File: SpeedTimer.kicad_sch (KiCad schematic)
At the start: 4 parts, among them Y1 ASCO

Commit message: Added 3.3v LDO. Increased page size. Added start/stop button circuit
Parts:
- added C2: 1n, symbol Device:C
- added C3: 2.2u, symbol Device:C
- added C4: .1u, symbol Device:C
- added D1: LED, symbol Device:LED
- added R10, R11, R3: 10K, symbol Device:R
- added R4: 600K, symbol Device:R
- added R5, R8: 1M, symbol Device:R
- added R6, R7: 47K, symbol Device:R
- added R9: 470, symbol Device:R
- added SW1, SW2, SW3: SW_Push, symbol Switch:SW_Push
- added U1, U2: 74LS393, symbol 74xx:74LS393
- added U3: 74HC74, symbol 74xx:74HC74
- added U4: KM28C64A, Package_DIP:DIP-28_W15.24mm, symbol Memory_EEPROM:KM28C64A
- added U5: 74HC173, symbol 74xx:74HC173
- added U6: LM317L_TO92, Package_TO_SOT_THT:TO-92_Inline, symbol Regulator_Linear:LM317L_TO92
- added U7: 74LS08, symbol 74xx:74LS08
- added U8: 74HC14, symbol 74xx:74HC14
- R1: value 1k -> 1K
- R2: value 1k -> 10K
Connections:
- net GND: now also C3.1, C4.1, D1.1 (K), R10.2, R11.2, R3.1, R5.2, R7.1, U1.7 (GND), U2.7 (GND), U3.7 (GND), U7.7 (GND), U8.7 (GND)
- net VDD: now also U1.14 (VCC), U2.14 (VCC), U3.14 (VCC), U7.14 (VCC), U8.14 (VCC); no longer R2.2, Y1.4 (VDD)
- net at C1.2, R1.1: now also R6.1, R7.2
- net at R1.2: now also U1.1 (CP)
- net CLK_32.768MHz: now reaches C1.1, Y1.3 (OUT)
- new net: R10.1, SW1.2, U7.4
- new net: U8.2, U8.3
- new net: U7.1, U8.4
- new net: R4.1, R5.1, U6.1 (ADJ)
- new net: C2.1, R3.2, U1.12 (MR), U1.2 (MR)
- new net: R8.2, R9.1, U7.10, U7.6
- new net: D1.2 (A), R9.2
- new net: C3.2, R8.1, U8.1
- new net: R11.1, SW2.2, U7.5
- new net: U1.13 (CP), U1.6 (Q3)
- new net +3.3V: C4.2, R2.2, R4.2, U6.2 (VO), Y1.4 (VDD)
- new net +5V: C2.2, R6.2, SW1.1, SW2.1, U3.4 (~{S}), U6.3 (VI)
- new net CLK_1kHz: U1.9 (Q2)
- new net SIG_START: U7.3
- new net SIG_STOP: U7.8
- new net TIMER_RUNNING: U3.5 (Q), U7.9
- new net ~{TIMER_RUNNING}: U3.2 (D), U3.6 (~{Q}), U7.2
- no-connect marks 0 -> 6
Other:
- moved on the sheet: C1, R1, R2, Y1

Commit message: Updated some triggering criteria
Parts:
- added C5, C6, C7: 1n, symbol Device:C
- added D4: LED, symbol Device:LED
- added Q1: NPN, symbol Simulation_SPICE:NPN
- added R12: 470, symbol Device:R
- added R13, R14, R15: 10K, symbol Device:R
- added U9: 74HC14, symbol 74xx:74HC14
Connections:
- net +3.3V: now also Q1.1 (C); no longer R2.2
- net +5V: now also SW3.1, U3.10 (~{S}), U3.12 (D), R13.1
- net GND: now also R2.1, R3.2, R9.2, R12.2, R14.2, R15.2; no longer D1.1 (K), R3.1
- net SIG_START: now also U8.6; no longer U7.3
- net SIG_STOP: now also C7.1, R14.1; no longer U7.8
- net TIMER_RUNNING: now also Q1.2 (B)
- net RESET: now reaches C2.1, U1.12 (MR), U1.2 (MR)
- net RESET: now also SW3.2, R15.1, U9.1; no longer R3.2
- net at R8.2, U7.10, U7.6: now also D1.2 (A); no longer R9.1
- net SIG_READY: now reaches U3.11 (C)
- net SIG_READY: now also R3.1, C5.1
- net ~{RESET}: now reaches U3.13 (~{R})
- net ~{RESET}: now also U3.1 (~{R}), U9.2
- net INIT: now reaches U3.8 (~{Q})
- net INIT: now also U7.13
- net READY: now reaches U3.9 (Q)
- net at U8.5: now also C6.1, R13.2
- net at Y1.1 (Tri-State): now also R2.2, Q1.3 (E); no longer R2.1
- net at U7.11: now also C5.2, C6.2, D4.2 (A)
- net at U7.12: now also U7.3
- new net: D1.1 (K), R9.1
- new net: C7.2, U7.8
- new net: D4.1 (K), R12.1
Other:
- moved on the sheet: C3, D1, R8, R9, U1B, U3A, U3B, U5, U7C, U7D, U8B, U8C

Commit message: Updated placement
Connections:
- net at C5.2, D4.2 (A), U7.11: no longer C6.2
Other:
- moved on the sheet: C2, C3, C5, C6, C7, D1, D4, R10, R11, R12, R13, R14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

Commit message: Filled out timer counter and started building out ALU
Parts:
- added D2, D3, D5, D6: D, symbol Device:D
- added R16: 10K, symbol Device:R
- added U10, U13: 74LS393, symbol 74xx:74LS393
- added U11, U12: CD4051B, symbol Analog_Switch:CD4051B
- added U14, U15: 74LS283, symbol 74xx:74LS283
- added U16: 74HC173, symbol 74xx:74HC173
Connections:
- net +3.3V: now also R16.2; no longer Q1.1 (C)
- net +5V: now also Q1.1 (C), U4.27 (~{WE}), U4.28 (VCC), U5.16 (VCC), U11.16 (VDD), U12.16 (VDD), U14.16 (VCC), U16.16 (VCC)
- net CLK_1kHz: now also U2.1 (CP)
- net CLK_32.768MHz: now also U5.7 (Cp), U13.1 (CP), U16.7 (Cp)
- net GND: now also D1.1 (K), D4.1 (K), U4.14 (GND), U4.2 (A12), U4.20 (~{CE}), U4.21 (A10), U4.22 (~{OE}), U4.23 (A11), U4.24 (A9), U4.25 (A8), U5.1 (Oe1), U5.10 (E2), U5.2 (Oe2), U5.8 (GND), U5.9 (E1), U10.7 (GND), U11.7 (VEE), U11.8 (VSS), U12.7 (VEE), U12.8 (VSS), U13.12 (MR), U13.2 (MR), U13.7 (GND), U14.8 (GND), U16.1 (Oe1), U16.10 (E2), U16.2 (Oe2), U16.8 (GND), U16.9 (E1); no longer R12.2, R9.2
- net INIT: now also D2.2 (A); no longer U7.13
- net READY: now also U7.1, D3.2 (A)
- net RESET: now also U2.12 (MR), U2.2 (MR), U10.12 (MR), U10.2 (MR); no longer U1.12 (MR), U1.2 (MR)
- net SIG_START: now also D5.2 (A)
- net SIG_STOP: now also D6.2 (A)
- net TIMER_RUNNING: no longer Q1.2 (B)
- net VDD: now also U10.14 (VCC), U13.14 (VCC)
- net ~{TIMER_RUNNING}: now also Q1.2 (B); no longer U7.2
- net at U8.4: now also C5.2, R12.1; no longer U7.1
- net at U2.10 (Q1): now also U11.5 (X5)
- net at U2.11 (Q0): now also U11.1 (X4)
- net at U2.13 (CP): now also U2.6 (Q3), U11.12 (X3)
- net at U2.8 (Q3): now also U10.1 (CP), U11.4 (X7)
- net at U2.9 (Q2): now also U11.2 (X6)
- net at R9.1: now also U7.10, U7.13, U7.6; no longer D1.1 (K)
- net at U5.11 (D3): now also U14.10 (S4)
- net at U5.12 (D2): now also U14.13 (S3)
- net at U5.13 (D1): now also U14.1 (S2)
- net at U5.14 (D0): now also U14.4 (S1)
- net at Q1.3 (E), R2.2: now also U1.12 (MR), U1.2 (MR); no longer Y1.1 (Tri-State)
- net at C6.2: now also U7.3
- net at U3.3 (C): now also D5.1 (K), D6.1 (K)
- net at U8.8: now also U12.6 (INH)
- net at U8.9: now also U4.7 (A3), U11.6 (INH), U13.13 (CP), U13.6 (Q3)
- net at U4.10 (A0): now also U11.11 (A), U12.11 (A), U13.3 (Q0)
- net at U4.11 (I/O0): now also U14.5 (A1)
- net at U4.12 (I/O1): now also U14.3 (A2)
- net at U4.13 (I/O2): now also U14.14 (A3)
- net at U4.15 (I/O3): now also U14.12 (A4)
- net at U4.3 (A7): now also U13.8 (Q3)
- net at U4.4 (A6): now also U13.9 (Q2)
- net at U4.5 (A5): now also U13.10 (Q1)
- net at U4.6 (A4): now also U13.11 (Q0)
- net at U4.8 (A2): now also U11.9 (C), U12.9 (C), U13.5 (Q2)
- net at U4.9 (A1): now also U11.10 (B), U12.10 (B), U13.4 (Q1)
- net at U2.3 (Q0): now also U11.13 (X0)
- net at U2.4 (Q1): now also U11.14 (X1)
- net at U2.5 (Q2): now also U11.15 (X2)
- net at U7.12: now also D2.1 (K), D3.1 (K); no longer U7.3
- net at U8.10: now also U7.2
- net at U8.11: now also R8.2, U7.11
- new net: U10.10 (Q1), U12.5 (X5)
- new net: U10.11 (Q0), U12.1 (X4)
- new net: U10.13 (CP), U10.6 (Q3), U12.12 (X3)
- new net: U10.8 (Q3), U12.4 (X7)
- new net: U10.9 (Q2), U12.2 (X6)
- new net: D1.2 (A), R9.2
- new net: R16.1, Y1.1 (Tri-State)
- new net: U10.3 (Q0), U12.13 (X0)
- new net: U10.4 (Q1), U12.14 (X1)
- new net: U10.5 (Q2), U12.15 (X2)
- new net: D4.2 (A), R12.2
- new net CURRENT_BIT: U11.3 (X), U12.3 (X)
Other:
- note added: "3.3V LDO"
- note added: "Clock Divider"
- note added: "Timer Counter"
- note added: "Timer Ready Control Bit"
- note added: "Timer Run Control Bit"
- note added: "Timer Start Control Flow"
- moved on the sheet: C1, C2, C3, C4, C5, C6, C7, D1, D4, Q1, R1, R10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

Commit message: Figured out ALU alignment
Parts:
- added U17: 74HC173, symbol 74xx:74HC173
- added U18: 74LS08, symbol 74xx:74LS08
- added U19: HDSP-7401, Display_7Segment:HDSP-7401, symbol Display_Character:HDSP-7401
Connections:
- net CURRENT_BIT is gone; now on an unnamed net: U11.3 (X), U12.3 (X)
- net +5V: now also U15.16 (VCC), U17.16 (VCC)
- net CLK_32.768MHz: now also U16.1 (Oe1), U5.1 (Oe1)
- net GND: now also U15.11 (B4), U15.12 (A4), U15.14 (A3), U15.15 (B3), U15.2 (B2), U15.3 (A2), U15.6 (B1), U15.8 (GND), U16.15 (Mr), U16.4 (Q1), U16.5 (Q2), U16.6 (Q3), U5.15 (Mr), U17.1 (Oe1), U17.10 (E2), U17.15 (Mr), U17.2 (Oe2), U17.8 (GND), U17.9 (E1), U18.7 (GND); no longer U16.1 (Oe1), U4.22 (~{OE}), U5.1 (Oe1)
- net VDD: now also U18.14 (VCC)
- net at U14.11 (B4): now also U5.6 (Q3), U17.11 (D3)
- net at U14.15 (B3): now also U5.5 (Q2), U17.12 (D2)
- net at U14.2 (B2): now also U5.4 (Q1), U17.13 (D1)
- net at U14.6 (B1): now also U5.3 (Q0), U17.14 (D0)
- net at U14.9 (C4): now also U15.7 (C0)
- net at U13.10 (Q1), U4.5 (A5): now also U18.2
- net at U13.9 (Q2), U4.4 (A6): now also U18.1
- net at U16.11 (D3): now also U15.10 (S4)
- net at U16.12 (D2): now also U15.13 (S3)
- net at U16.13 (D1): now also U15.1 (S2)
- net at U16.14 (D0): now also U15.4 (S1)
- net at U16.3 (Q0): now also U15.5 (A1)
- net at U8.12: now also U4.22 (~{OE})
- new net: U17.7 (Cp), U18.3
- no-connect marks 6 -> 10
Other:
- moved on the sheet: U13B, U15, U16, U5, U8F, U8G

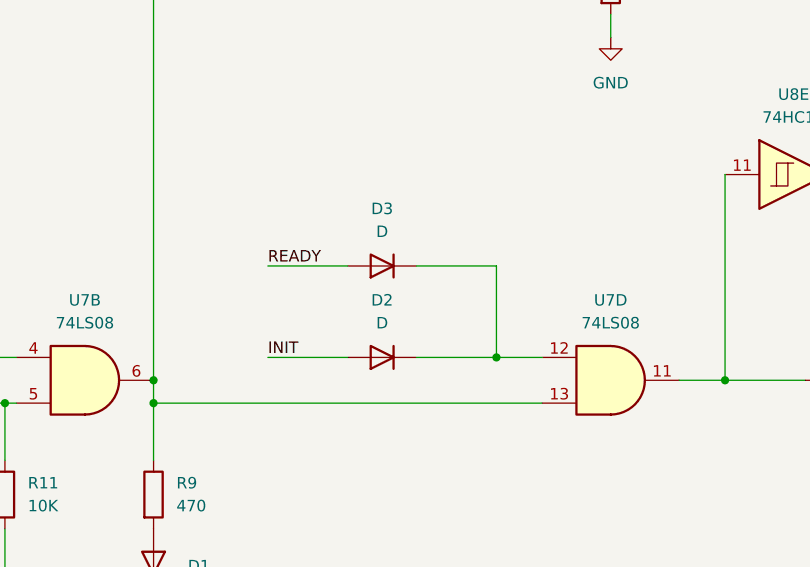
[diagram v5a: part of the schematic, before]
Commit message: Updated gitignore to ignore -bak files
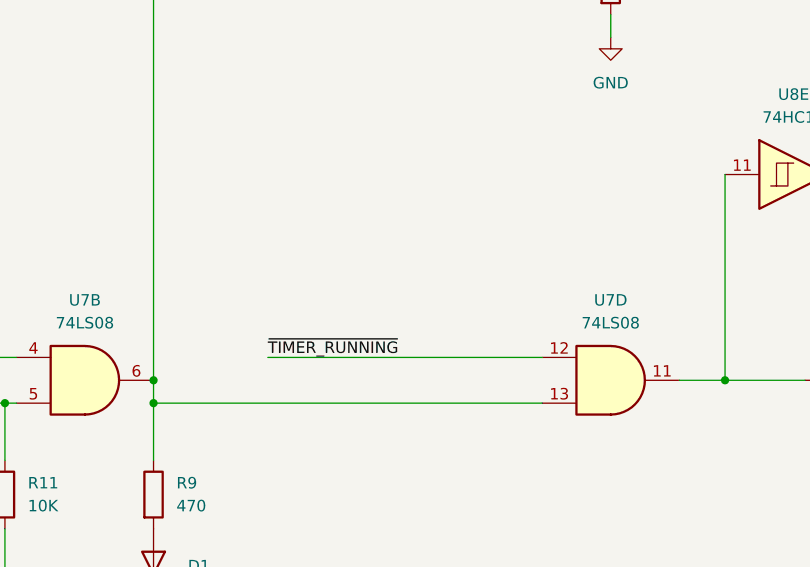
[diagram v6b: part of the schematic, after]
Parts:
- removed D2, D3: D, symbol Device:D
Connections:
- net ~{TIMER_RUNNING}: now also U7.12
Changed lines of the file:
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@@
 	)
 	(junction
-		(at 101.6 365.76)
-		(diameter 0)
-		(color 0 0 0 0)
-	)
-	(junction
 		(at 408.94 182.88)
 		(diameter 0)
@@
 	(wire
 		(pts
-			(xy 85.09 365.76) (xy 76.2 365.76)
-		)
-		(stroke
-			(width 0)
-			(type default)
-		)
-	)
-	(wire
-		(pts
 			(xy 317.5 111.76) (xy 322.58 111.76)
 		)
@@
 	(wire
 		(pts
-			(xy 101.6 365.76) (xy 106.68 365.76)
-		)
-		(stroke
-			(width 0)
-			(type default)
-		)
-	)
-	(wire
-		(pts
 			(xy 337.82 -29.21) (xy 327.66 -29.21)
 		)
@@
 	(wire
 		(pts
-			(xy 92.71 355.6) (xy 101.6 355.6)
-		)
-		(stroke
-			(width 0)
-			(type default)
-		)
-	)
-	(wire
-		(pts
 			(xy 323.85 151.13) (xy 322.58 151.13)
 		)
@@
 	(wire
 		(pts
-			(xy 92.71 365.76) (xy 101.6 365.76)
-		)
-		(stroke
-			(width 0)
-			(type default)
-		)
-	)
-	(wire
-		(pts
 			(xy 208.28 342.9) (xy 203.2 342.9)
 		)
@@
 	(wire
 		(pts
+			(xy 76.2 365.76) (xy 106.68 365.76)
+		)
+		(stroke
+			(width 0)
+			(type default)
+		)
+	)
+	(wire
+		(pts
 			(xy 50.8 38.1) (xy 63.5 38.1)
 		)
@@
 	(wire
 		(pts
-			(xy 76.2 355.6) (xy 85.09 355.6)
-		)
-		(stroke
-			(width 0)
-			(type default)
-		)
-	)
-	(wire
-		(pts
 			(xy 419.1 177.8) (xy 406.4 177.8)
 		)
@@
 	(wire
 		(pts
-			(xy 101.6 355.6) (xy 101.6 365.76)
-		)
-		(stroke
-			(width 0)
-			(type default)
-		)
-	)
-	(wire
-		(pts
 			(xy 58.42 134.62) (xy 58.42 198.12)
 		)
@@
 		)
 	)
+	(label "~{TIMER_RUNNING}"
+		(at 76.2 365.76 0)
+		(effects
+			(font
+				(size 1.27 1.27)
+			)
+			(justify left bottom)
+		)
+	)
 	(label "~{RESET}"
 		(at 165.1 276.86 0)
@@
 		)
 	)
-	(label "READY"
-		(at 76.2 355.6 0)
-		(effects
-			(font
-				(size 1.27 1.27)
-			)
-			(justify left bottom)
-		)
-	)
 	(label "~{TIMER_RUNNING}"
 		(at 139.7 264.16 0)
@@
 		)
 	)
-	(label "INIT"
-		(at 76.2 365.76 0)
-		(effects
-			(font
-				(size 1.27 1.27)
-			)
-			(justify left bottom)
-		)
-	)
 	(label "~{RESET}"
 		(at 337.82 -29.21 180)
@@
 					(unit 1)
 				)
-			)
-		)
-	)
-	(symbol
-		(lib_id "Device:D")
-		(at 88.9 365.76 180)
-		(unit 1)
-		(exclude_from_sim no)
-		(in_bom yes)
-		(on_board yes)
-		(dnp no)
-		(fields_autoplaced yes)
-		(property "Reference" "D2"
-			(at 88.9 359.41 0)
-			(effects
-				(font
-					(size 1.27 1.27)
-				)
-			)
-		)
-		(property "Value" "D"
-			(at 88.9 361.95 0)
-			(effects
-				(font
-					(size 1.27 1.27)
-				)
-			)
-		)
-		(property "Footprint" ""
-			(at 88.9 365.76 0)
-			(effects
-				(font
-					(size 1.27 1.27)
-				)
-				(hide yes)
-			)
-		)
-		(property "Datasheet" "~"
-			(at 88.9 365.76 0)
-			(effects
-				(font
-					(size 1.27 1.27)
-				)
-				(hide yes)
-			)
-		)
-		(property "Description" "Diode"
-			(at 88.9 365.76 0)
-			(effects
-				(font
-					(size 1.27 1.27)
-				)
-				(hide yes)
-			)
-		)
-		(property "Sim.Device" "D"
-			(at 88.9 365.76 0)
-			(effects
-				(font
-					(size 1.27 1.27)
-				)
-				(hide yes)
-			)
-		)
-		(property "Sim.Pins" "1=K 2=A"
-			(at 88.9 365.76 0)
-			(effects
-				(font
-					(size 1.27 1.27)
-				)
-				(hide yes)
-			)
-		)
-		(pin "2"
-		)
-		(pin "1"
-		)
-		(instances
-			(project ""
-				(path "/01ea14ff-2ec7-4859-9809-aee58bc13c38"
-					(reference "D2")
-					(unit 1)
-				)
-			)
-		)
-	)
-	(symbol
-		(lib_id "Device:D")
-		(at 88.9 355.6 180)
-		(unit 1)
-		(exclude_from_sim no)
-		(in_bom yes)
-		(on_board yes)
-		(dnp no)
-		(fields_autoplaced yes)
-		(property "Reference" "D3"
-			(at 88.9 349.25 0)
-			(effects
-				(font
-					(size 1.27 1.27)
-				)
-			)
-		)
-		(property "Value" "D"
-			(at 88.9 351.79 0)
-			(effects
-				(font
-					(size 1.27 1.27)
-				)
-			)
-		)
-		(property "Footprint" ""
-			(at 88.9 355.6 0)
-			(effects
-				(font
-					(size 1.27 1.27)
-				)
-				(hide yes)
-			)
-		)
-		(property "Datasheet" "~"
-			(at 88.9 355.6 0)
-			(effects
-				(font
-					(size 1.27 1.27)
-				)
-				(hide yes)
-			)
-		)
-		(property "Description" "Diode"
-			(at 88.9 355.6 0)
-			(effects
-				(font
-					(size 1.27 1.27)
-				)
-				(hide yes)
-			)
-		)
-		(property "Sim.Device" "D"
-			(at 88.9 355.6 0)
-			(effects
-				(font
-					(size 1.27 1.27)
-				)
-				(hide yes)
-			)
-		)
-		(property "Sim.Pins" "1=K 2=A"
-			(at 88.9 355.6 0)
-			(effects
-				(font
-					(size 1.27 1.27)
-				)
-				(hide yes)
-			)
-		)
-		(pin "2"
-		)
-		(pin "1"
-		)
-		(instances
-			(project "SpeedTimer"
-				(path "/01ea14ff-2ec7-4859-9809-aee58bc13c38"
-					(reference "D3")
-					(unit 1)
-				)
